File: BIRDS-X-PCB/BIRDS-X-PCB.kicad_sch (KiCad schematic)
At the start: 9 parts, among them J101 LPC-50M2LG, J102 RFShield_OnePiece, J103 RFShield_OnePiece, J104 RFShield_OnePiece

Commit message: Fix logo
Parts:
- added H105: Logo, BIRDS-X_Footprints_Lib:AlbertaSat_Logo_25x20mm, symbol Mechanical:MountingHole
- added H106: Logo, BIRDS-X_Footprints_Lib:CTS_Logo_50x25mm, symbol Mechanical:MountingHole
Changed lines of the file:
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@@
+    )
+  )
+  (symbol (lib_id "Mechanical:MountingHole") (at 50.8 184.15 0) (unit 1)
+    (in_bom yes) (on_board yes) (dnp no) (fields_autoplaced)
+    (property "Reference" "H106" (at 53.34 182.88 0)
+      (effects (font (size 1.27 1.27)) (justify left))
+    )
+    (property "Value" "Logo" (at 53.34 185.42 0)
+      (effects (font (size 1.27 1.27)) (justify left))
+    )
+    (property "Footprint" "BIRDS-X_Footprints_Lib:CTS_Logo_50x25mm" (at 50.8 184.15 0)
+      (effects (font (size 1.27 1.27)) hide)
+    )
+    (property "Datasheet" "~" (at 50.8 184.15 0)
+      (effects (font (size 1.27 1.27)) hide)
+    )
+    (instances
+      (project "BIRDS-X-PCB"
+        (path "/c2796b15-795a-4d6e-ad4b-0ba87ded4bc9"
+          (reference "H106") (unit 1)
+        )
+      )
     )
   )
@@
         )
       )
+    )
+  )
+  (symbol (lib_id "Mechanical:MountingHole") (at 50.8 179.07 0) (unit 1)
+    (in_bom yes) (on_board yes) (dnp no) (fields_autoplaced)
+    (property "Reference" "H105" (at 53.34 177.8 0)
+      (effects (font (size 1.27 1.27)) (justify left))
+    )
+    (property "Value" "Logo" (at 53.34 180.34 0)
+      (effects (font (size 1.27 1.27)) (justify left))
+    )
+    (property "Footprint" "BIRDS-X_Footprints_Lib:AlbertaSat_Logo_25x20mm" (at 50.8 179.07 0)
+      (effects (font (size 1.27 1.27)) hide)
+    )
+    (property "Datasheet" "~" (at 50.8 179.07 0)
+      (effects (font (size 1.27 1.27)) hide)
+    )
+    (instances
+      (project "BIRDS-X-PCB"
+        (path "/c2796b15-795a-4d6e-ad4b-0ba87ded4bc9"
+          (reference "H105") (unit 1)
+        )
+      )

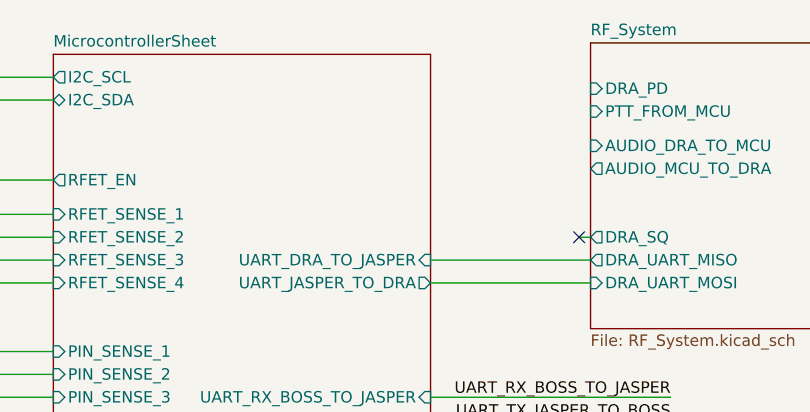
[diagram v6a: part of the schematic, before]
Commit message: Fix missing connections, release Rev5.0
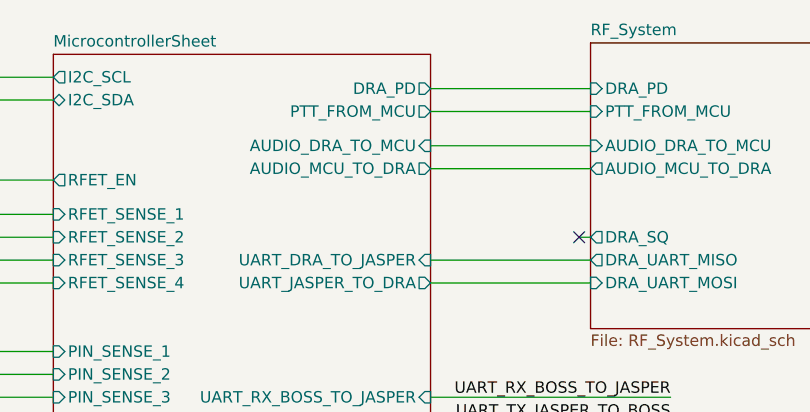
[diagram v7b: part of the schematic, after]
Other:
- sheet MicrocontrollerSheet ports: added AUDIO_DRA_TO_MCU, AUDIO_MCU_TO_DRA, DRA_PD, PTT_FROM_MCU; removed none
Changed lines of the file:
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@@
 (kicad_sch (version 20230121) (generator eeschema)
   (paper "USLetter")
+  (title_block
+    (date "2023-08-23")
+    (rev "Rev5.0")
+  )
   (junction (at 181.61 118.11) (diameter 0) (color 0 0 0 0)
   )
@@
     (stroke (width 0) (type default))
   )
+  (wire (pts (xy 187.96 24.13) (xy 205.74 24.13))
+    (stroke (width 0) (type default))
+  )
   (wire (pts (xy 83.82 33.02) (xy 83.82 38.1))
     (stroke (width 0) (type default))
@@
     (stroke (width 0) (type default))
   )
+  (wire (pts (xy 187.96 21.59) (xy 205.74 21.59))
+    (stroke (width 0) (type default))
+  )
   (wire (pts (xy 187.96 40.64) (xy 205.74 40.64))
     (stroke (width 0) (type default))
@@
     (stroke (width 0) (type default))
   )
+  (wire (pts (xy 187.96 30.48) (xy 205.74 30.48))
+    (stroke (width 0) (type default))
+  )
   (wire (pts (xy 175.26 87.63) (xy 181.61 87.63))
     (stroke (width 0) (type default))
@@
   )
   (wire (pts (xy 83.82 38.1) (xy 76.2 38.1))
+    (stroke (width 0) (type default))
+  )
+  (wire (pts (xy 187.96 27.94) (xy 205.74 27.94))
     (stroke (width 0) (type default))
   )
@@
       (effects (font (size 1.27 1.27)) (justify left))
     )
-    (instances
+    (pin "AUDIO_MCU_TO_DRA" output (at 187.96 30.48 0)
+      (effects (font (size 1.27 1.27)) (justify right))
+    )
+    (pin "PTT_FROM_MCU" output (at 187.96 24.13 0)
+      (effects (font (size 1.27 1.27)) (justify right))
+    )
+    (pin "DRA_PD" output (at 187.96 21.59 0)
+      (effects (font (size 1.27 1.27)) (justify right))
+    )
+    (pin "AUDIO_DRA_TO_MCU" input (at 187.96 27.94 0)
+      (effects (font (size 1.27 1.27)) (justify right))
+    )
+    (instances

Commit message: Prep docs for Rev5.1 release
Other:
- note added: "Rev5.1: All Open"
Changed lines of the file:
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@@
   (paper "USLetter")
   (title_block
-    (date "2023-08-23")
-    (rev "Rev5.0")
+    (date "2023-09-07")
+    (rev "Rev5.1")
   )
   (junction (at 181.61 118.11) (diameter 0) (color 0 0 0 0)
@@
     (effects (font (size 1.27 1.27)) (justify left bottom))
   )
+  (text "Rev5.1: All Open" (at 62.23 34.29 0)
+    (effects (font (size 1.27 1.27)) (justify left bottom))
+  )
